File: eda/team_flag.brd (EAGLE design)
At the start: 40.6 x 40.6 mm, 22 parts, among them Q1 IRFML8244, Q2 IRFML8244, U1 ISL83491SOIC, U2 ATTINY1634

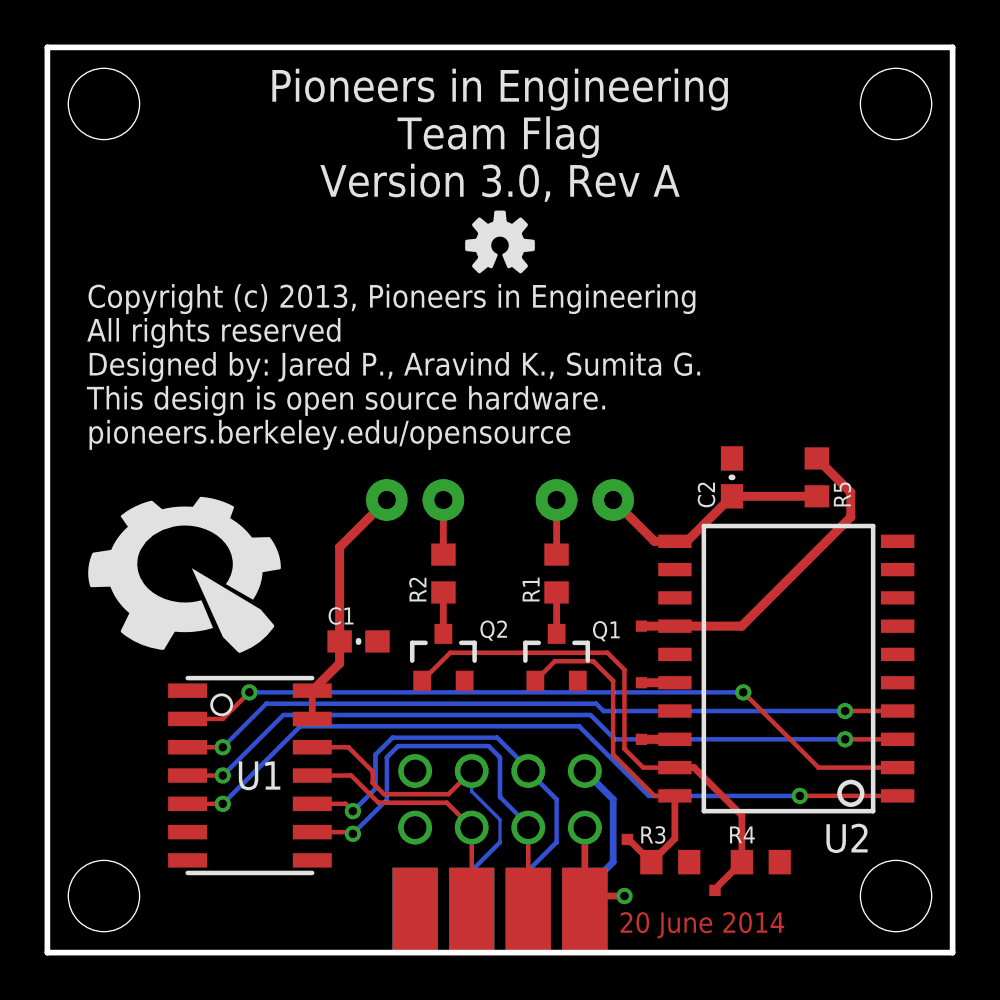
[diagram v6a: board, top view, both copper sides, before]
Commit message: Correct rev, version #, and dates on all boards!
Plus a few other minor changes:
- Standardized silk screen style across jigs.
- Fixed wierd trace angles.
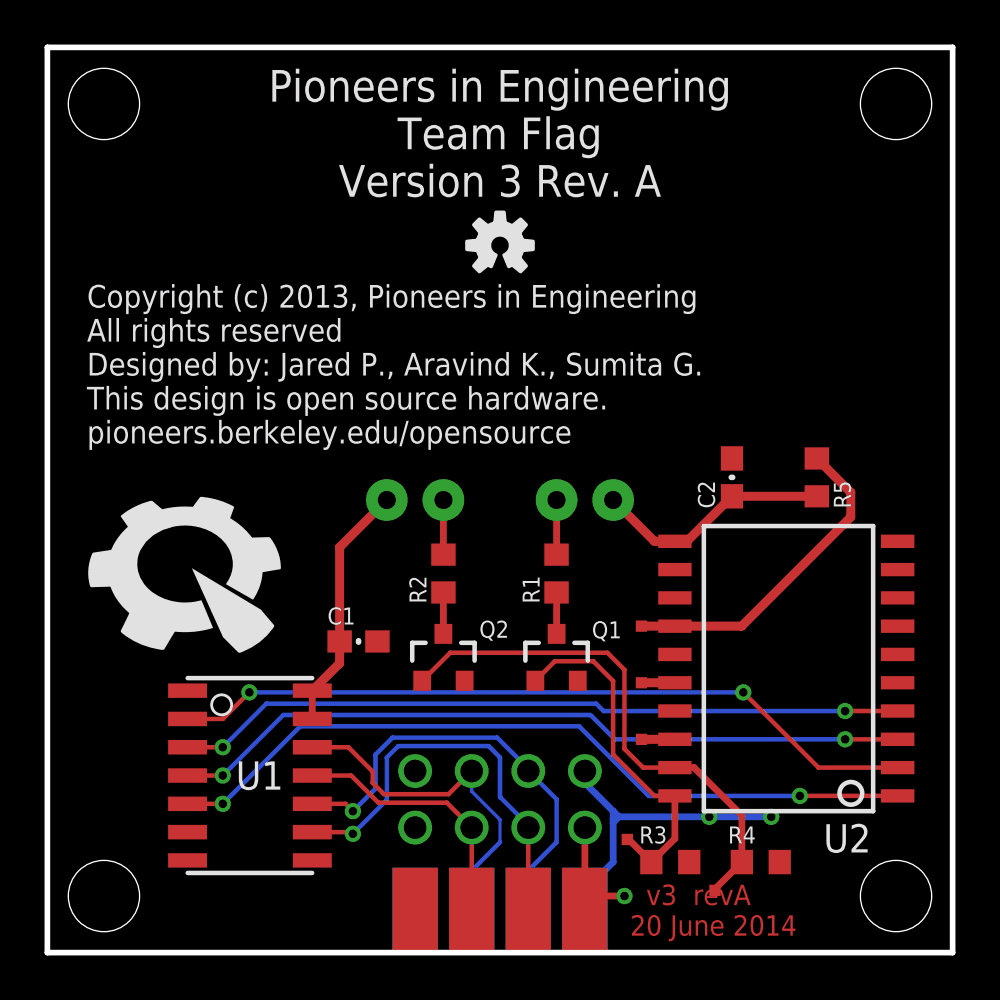
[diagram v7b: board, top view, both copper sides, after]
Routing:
- net GND: track 7.30 -> 15.2 mm, vias 0 -> 2
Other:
- board text added: "Pioneers in Engineering Team Flag Version 3 Rev. A"
- board text added: "v3 revA 20 June 2014"
- board text removed: "20 June 2014"
- board text removed: "Pioneers in Engineering Team Flag Version 3.0, Rev A"
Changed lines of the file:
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@@
 <layer number="19" name="Unrouted" color="6" fill="1" visible="yes" active="yes"/>
 <layer number="20" name="Dimension" color="15" fill="1" visible="yes" active="yes"/>
-<layer number="21" name="tPlace" color="16" fill="1" visible="no" active="yes"/>
+<layer number="21" name="tPlace" color="16" fill="1" visible="yes" active="yes"/>
 <layer number="22" name="bPlace" color="17" fill="1" visible="yes" active="yes"/>
 <layer number="23" name="tOrigins" color="15" fill="1" visible="yes" active="yes"/>
 <layer number="24" name="bOrigins" color="15" fill="1" visible="yes" active="yes"/>
-<layer number="25" name="tNames" color="18" fill="1" visible="no" active="yes"/>
+<layer number="25" name="tNames" color="18" fill="1" visible="yes" active="yes"/>
 <layer number="26" name="bNames" color="19" fill="1" visible="yes" active="yes"/>
-<layer number="27" name="tValues" color="18" fill="1" visible="no" active="yes"/>
+<layer number="27" name="tValues" color="18" fill="1" visible="yes" active="yes"/>
 <layer number="28" name="bValues" color="19" fill="1" visible="yes" active="yes"/>
 <layer number="29" name="tStop" color="7" fill="3" visible="no" active="yes"/>
@@
 <text x="16.764" y="39.624" size="1.4224" layer="21" font="vector" ratio="15" rot="R180" align="bottom-center">Pioneers in Engineering
 Team Flag
-Version 3.0, Rev A</text>
+Version 3 Rev. A</text>
 <text x="-1.778" y="29.972" size="1.016" layer="21" font="vector" ratio="15" align="top-left">Copyright (c) 2013, Pioneers in Engineering
 All rights reserved
@@
 This design is open source hardware.
 pioneers.berkeley.edu/opensource</text>
-<text x="22.098" y="0.889" size="0.9144" layer="1" font="vector" ratio="20">20 June 2014</text>
+<text x="22.606" y="0.762" size="0.9144" layer="1" font="vector" ratio="20">  v3  revA
+20 June 2014</text>
 </plain>
 <attributes>
@@
 <element name="R3" library="pie" package="R0603" value="10k" x="24.4094" y="4.064" smashed="yes" rot="R180">
 <attribute name="NAME" x="23.0124" y="4.9022" size="0.762" layer="25" font="vector" ratio="15"/>
-<attribute name="VALUE" x="23.0124" y="2.4638" size="0.762" layer="27" font="vector" ratio="15"/>
+<attribute name="VALUE" x="24.7904" y="4.8768" size="0.762" layer="27" font="vector" ratio="15"/>
 <attribute name="PIE-INT-REF-NUM" value="RESISTOR-GENERIC" x="24.4094" y="4.064" size="1.778" layer="27" rot="R180" display="off"/>
 </element>
 <element name="R4" library="pie" package="R0603" value="10k" x="28.4734" y="4.064" smashed="yes" rot="R180">
 <attribute name="NAME" x="27.0002" y="4.9022" size="0.762" layer="25" font="vector" ratio="15" rot="R180" align="top-right"/>
-<attribute name="VALUE" x="27.1272" y="2.4638" size="0.762" layer="27" font="vector" ratio="15" rot="R180" align="top-right"/>
+<attribute name="VALUE" x="28.7782" y="4.8768" size="0.762" layer="27" font="vector" ratio="15" rot="R180" align="top-right"/>
 <attribute name="PIE-INT-REF-NUM" value="RESISTOR-GENERIC" x="28.4734" y="4.064" size="1.778" layer="27" rot="R180" display="off"/>
 </element>
@@
 <vertex x="37.084" y="40.64"/>
 </polygon>
-<wire x1="20.574" y1="8.1534" x2="21.844" y2="6.8834" width="0.3048" layer="16"/>
-<wire x1="21.844" y1="6.8834" x2="21.844" y2="4.064" width="0.3048" layer="16"/>
 <wire x1="21.844" y1="4.064" x2="20.574" y2="2.794" width="0.3048" layer="16"/>
 <wire x1="20.574" y1="2.794" x2="20.574" y2="1.905" width="0.3048" layer="16"/>
+<wire x1="25.2594" y1="4.064" x2="25.273" y2="4.064" width="0.3048" layer="1"/>
+<wire x1="26.162" y1="6.096" x2="28.9424" y2="6.096" width="0.3048" layer="16"/>
+<via x="26.162" y="6.096" extent="1-16" drill="0.381"/>
+<via x="28.9424" y="6.096" extent="1-16" drill="0.381"/>
+<wire x1="21.844" y1="6.35" x2="20.574" y2="7.62" width="0.3048" layer="16"/>
+<wire x1="20.574" y1="7.62" x2="20.574" y2="8.1534" width="0.3048" layer="16"/>
+<wire x1="21.844" y1="4.064" x2="21.844" y2="5.842" width="0.3048" layer="16"/>
+<wire x1="21.844" y1="5.969" x2="21.844" y2="6.35" width="0.3048" layer="16"/>
+<wire x1="21.844" y1="6.35" x2="22.098" y2="6.096" width="0.3048" layer="16"/>
+<wire x1="22.098" y1="6.096" x2="21.844" y2="5.842" width="0.3048" layer="16"/>
+<wire x1="21.844" y1="5.842" x2="21.844" y2="5.969" width="0.3048" layer="16"/>
+<wire x1="21.844" y1="5.969" x2="21.971" y2="6.096" width="0.3048" layer="16"/>
+<wire x1="21.971" y1="6.096" x2="26.162" y2="6.096" width="0.3048" layer="16"/>
 </signal>
 <signal name="BLUE">

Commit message: Ribboncable pinout fixed.
On battery_buzzer, smartsensor, and smartsensorPowered.
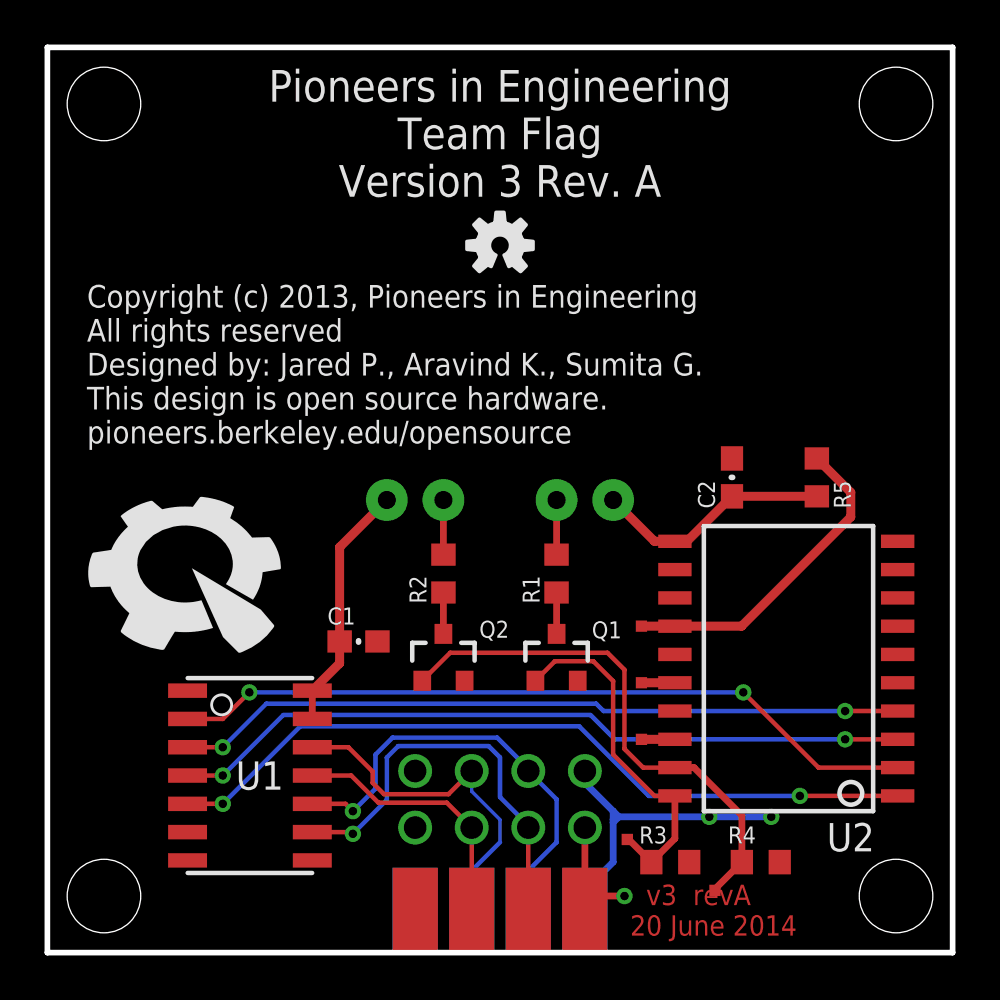
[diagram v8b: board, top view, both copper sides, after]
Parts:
- added U$11, U$12, U$13, U$14: (no value), pie:STAND-OFF
- U2: device pie:SOIC20S -> pie:SOIC20
- moved U2 7.41 mm to (29.6, 12.8), turned to 180 degrees
